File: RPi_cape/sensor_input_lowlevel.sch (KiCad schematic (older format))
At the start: 38 parts, among them U14 DNP, U15 LMC7101B, U16 LMC7101B, U17 LM2903

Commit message: Finished schematic, most of PCB placement
Added error budget for analog inputs
Finished most of PCB placement and started routing
Added R185, R186 to allow powering CPLD from alarm power for better power-down alarm sound flexibility
Changed power-down alarm monitoring from +5VD to +3.3V, and put +5VA and +24VA monitoring as DNP by default, to match the CPLD's ability to run off backup battery and monitor +5VA/+24VA
Moved from 3x AA (4.5V) to 4x AA (6V) alarm battery for better audio voltage, and added PNP diode-ORing circuit (Q12 etc.) to accomodate higher voltage, changed low-battery threshold to 5V
Added pull-down resistors to sensor op-amp outputs to help extend low-end output range
Changed 1nF, 10nF, 100nF caps to 0603-size for better fit of CPLD decoupling caps
Added additional bulk cap C19 to audio amp's supply just in case of alarm-induced supply fluctuations
Decreased CPLD's I2C pull-up values to deal with anticipated PCB capacitance etc.
Removed additional dual-op-amp footprint option on analog inputs, due to high availability of single op-amps
Adjusted O2 sensor input clamping to reduce errors from diode leakage current (changed from zener to low-leakage clamps to rails)
Changed O2 sensor op-amp to different lower-offset part to reduce total error from +/- 4.2% FS to +/- 1.7% FS
Fixed missing power section for U17
Added rotary encoder input
Consolidated +5VA fuse options
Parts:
- removed C40, C43: 1uF 16V X7R, Capacitor_SMD:C_0805_2012Metric, symbol Device:C
- removed U14: DNP, Package_SO:SOIC-8_3.9x4.9mm_P1.27mm, symbol Device:Opamp_Dual_Generic
- removed U15, U16: LMC7101B, Package_TO_SOT_SMD:SOT-23-5, symbol Amplifier_Operational:LMV321
- added C31: 1uF 16V X7R, Capacitor_SMD:C_0805_2012Metric, symbol Device:C
- added R183, R184: 10K, Resistor_SMD:R_1206_3216Metric, symbol Device:R
- added unit 3 of U17
- added U4: AD8552A, Package_SO:SOIC-8_3.9x4.9mm_P1.27mm, symbol Device:Opamp_Dual_Generic
- C41, C44, C45: footprint Capacitor_SMD:C_0805_2012Metric -> Capacitor_SMD:C_0603_1608Metric; Manufacturer Samsung -> Murata; Part Number CL21C103JBFNNNG -> GRM1885C1H103JA01D
- C46, C47: footprint Capacitor_SMD:C_0805_2012Metric -> Capacitor_SMD:C_0603_1608Metric; Part Number 08055C104KAT2A -> 06035C104JAT2A
- D19: value DNP -> BAS21AH; footprint Diode_SMD:D_SOD-123 -> Diode_SMD:D_SOD-323; Manufacturer (none) -> ON Semiconductor; Part Number (none) -> BAS21AHT1G
- D20: value 5.1V -> BAS21AH; footprint Diode_SMD:D_SOD-123 -> Diode_SMD:D_SOD-323; symbol Device:D_Zener_ALT -> Device:D_ALT; Manufacturer (none) -> ON Semiconductor; Part Number (none) -> BAS21AHT1G
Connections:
- net +5VA: now also C31.2, U17.8 (V+), U4.8 (V+)
- net GND: now also C31.1, R183.1, R184.1, U17.4 (V-), U4.4 (V-)
- net Out: now also R183.2, U4.1
- net at R87.1: now also U4.5 (+)
- net at C45.1, R91.1, R92.2: now also R184.2, U4.7
- net at C45.2, R89.2, R91.2: now also U4.6 (-)
- net at R86.1: now also U4.3 (+)
- net at C44.2, R88.2, R90.2: now also U4.2 (-)
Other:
- note added: "Gain of +101 (7 mV in = 0.707V out, 13 mV in = 1.31V out)\nLPF fc = 1.6 kHz"
- note removed: "Gain of +101 (21 mV in = 2.12V out)\nLPF fc = 1.6 kHz"
- moved on the sheet: C42, R87, R88, R89

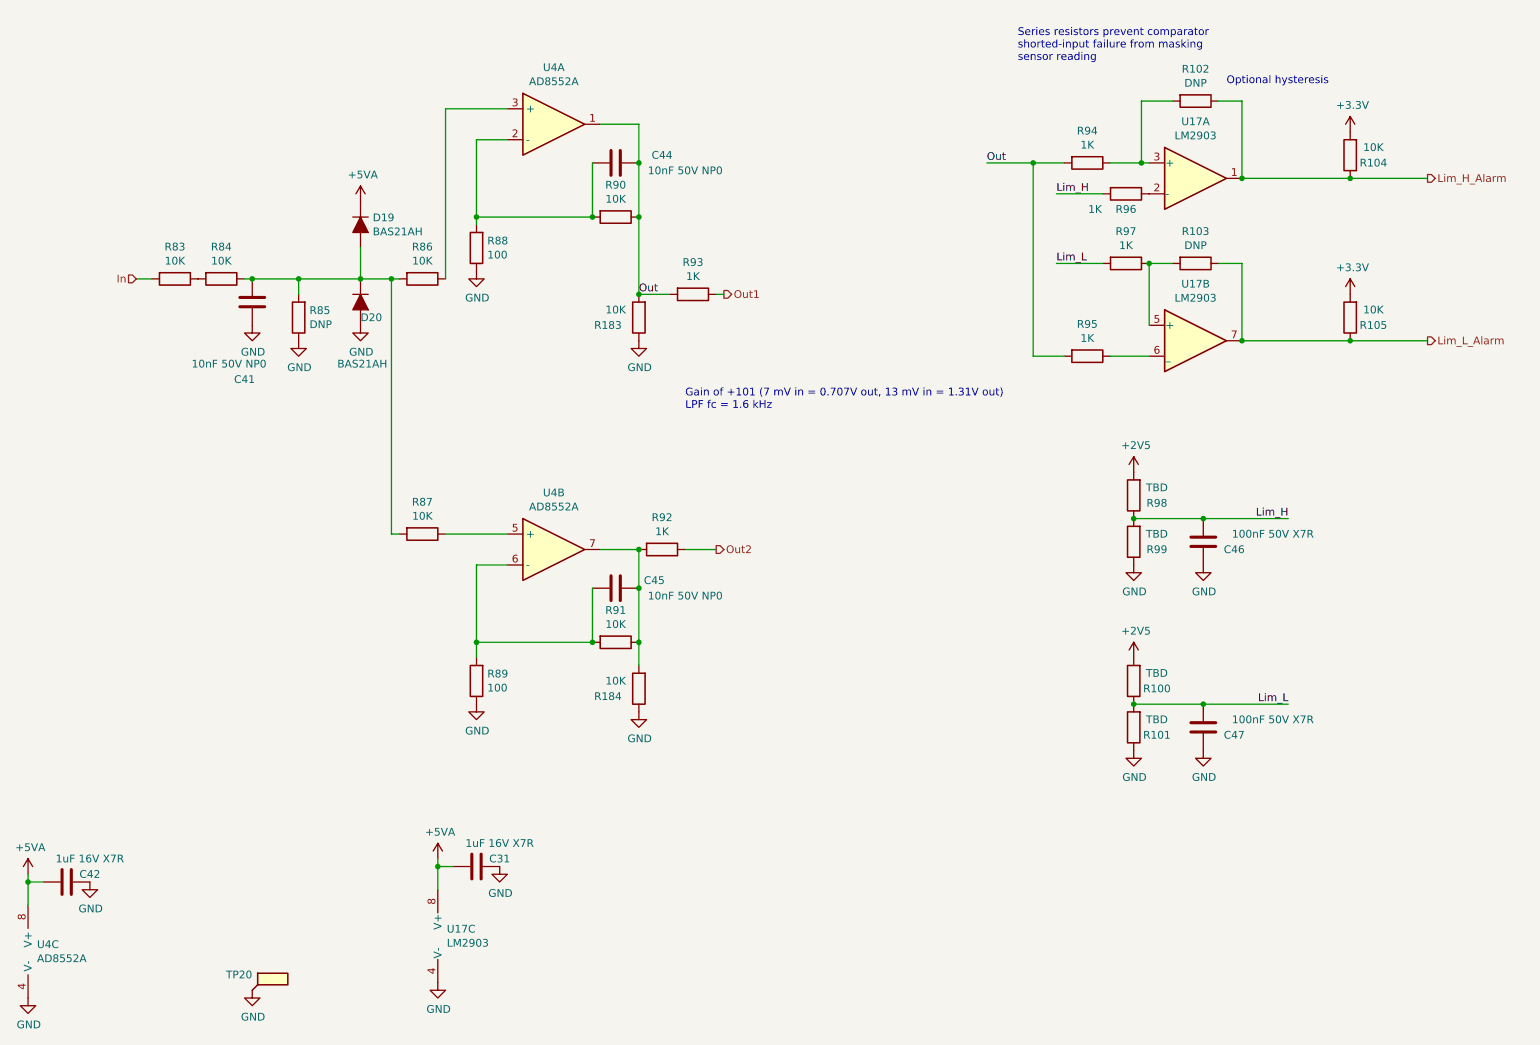
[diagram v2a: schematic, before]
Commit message: Better valve monitoring, finalized layout and manufacturing files
Created assembly and fabrication drawings, assigned all BOM parts, generally made design ready for ordering
Added strain-relief slots and barb mounting dimensions for digital pressure sensors
Changed valve drivers from discrete power MOSFETs to "smart" industrial/automotive driver ICs for the current monitoring, including valve-movement monitor for #4
Connected RPi_Valve* signals to larger CPLD footprint, changed Raspberry Pi pin assignment as a result to ease PCB routing
Updated footprints, page layout to create readable assembly drawing
Added current-measurement testpoints for CPLD power from BATT+
Changed power diodes in power-down-alarm circuit to small-signal parts for more compact layout
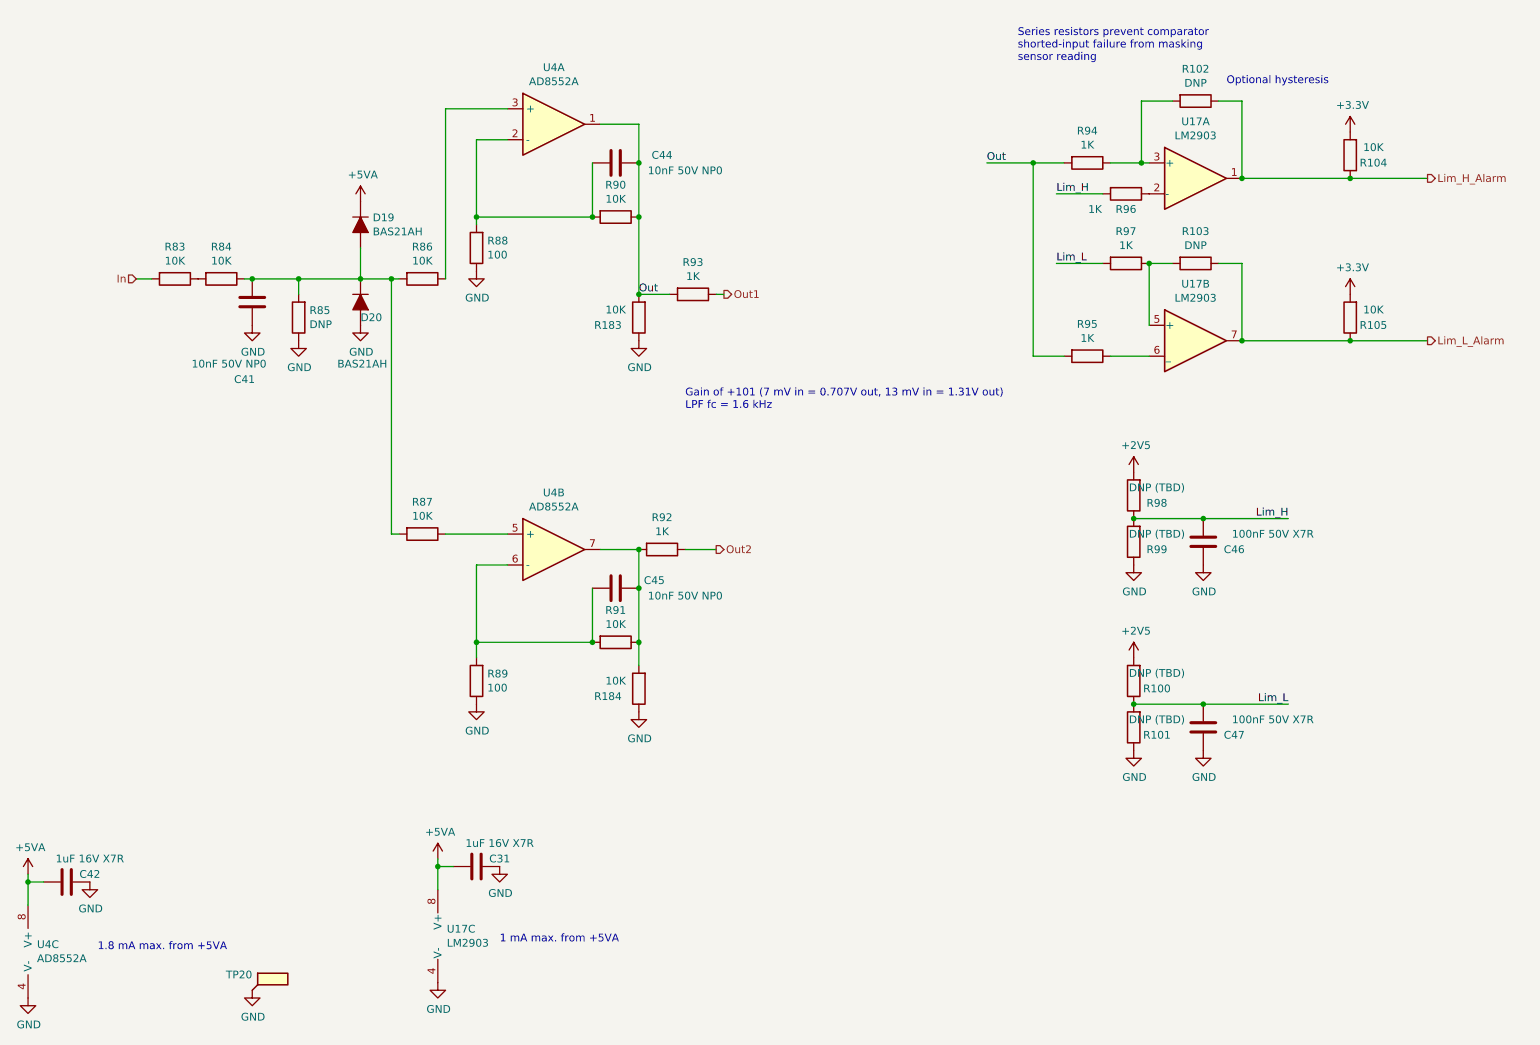
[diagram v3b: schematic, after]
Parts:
- D19, D20: footprint Diode_SMD:D_SOD-323 -> Ventilator:D_SOD-323
- R100, R101, R98, R99: value TBD -> DNP (TBD)
- R104, R105, R183, R184, R83, R84, R86, R87, R90, R91: Manufacturer (none) -> KOA Speer; Part Number (none) -> RK73H2BTTD1002F
- R88, R89: Manufacturer (none) -> KOA Speer; Part Number (none) -> RK73H2BTTD1000F
- R92, R93, R94, R95, R96, R97: Manufacturer (none) -> KOA Speer; Part Number (none) -> RK73H2BTTD1001F
- U17: footprint Package_SO:VSSOP-8_3.0x3.0mm_P0.65mm -> Ventilator:VSSOP-8_3.0x3.0mm_P0.65mm
- U4: footprint Package_SO:SOIC-8_3.9x4.9mm_P1.27mm -> Ventilator:SOIC-8_3.9x4.9mm_P1.27mm
- U4: footprint Package_SO:SOIC-8_3.9x4.9mm_P1.27mm -> Ventilator:SOIC-8_3.9x4.9mm_P1.27mm; Manufacturer (none) -> Analog Devices; Part Number (none) -> AD8552ARZ-REEL
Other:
- note added: "1 mA max. from +5VA"
- note added: "1.8 mA max. from +5VA"
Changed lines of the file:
@@
 $Descr A4 11693 8268
 encoding utf-8
-Sheet 5 14
+Sheet 5 15
 Title "Sensor Input (low-level oxygen sensor)"
 Date ""
@@
 F 2 "Resistor_SMD:R_1206_3216Metric" V 3530 4250 50  0001 C CNN
 F 3 "~" H 3600 4250 50  0001 C CNN
+F 4 "KOA Speer" H 3600 4250 50  0001 C CNN "Manufacturer"
+F 5 "RK73H2BTTD1002F" H 3600 4250 50  0001 C CNN "Part Number"
 	1    3600 4250
 	0    1    1    0
@@
 F 2 "Resistor_SMD:R_1206_3216Metric" V 3880 5200 50  0001 C CNN
 F 3 "~" H 3950 5200 50  0001 C CNN
+F 4 "KOA Speer" H 3950 5200 50  0001 C CNN "Manufacturer"
+F 5 "RK73H2BTTD1000F" H 3950 5200 50  0001 C CNN "Part Number"
 	1    3950 5200
 	-1   0    0    1
@@
 F 2 "Resistor_SMD:R_1206_3216Metric" V 4780 4950 50  0001 C CNN
 F 3 "~" H 4850 4950 50  0001 C CNN
+F 4 "KOA Speer" H 4850 4950 50  0001 C CNN "Manufacturer"
+F 5 "RK73H2BTTD1002F" H 4850 4950 50  0001 C CNN "Part Number"
 	1    4850 4950
 	0    1    1    0
@@
 F 0 "D20" V 3300 2750 50  0000 L CNN
 F 1 "BAS21AH" V 3600 2600 50  0000 L CNN
-F 2 "Diode_SMD:D_SOD-323" H 3200 2750 50  0001 C CNN
+F 2 "Ventilator:D_SOD-323" H 3200 2750 50  0001 C CNN
 F 3 "~" H 3200 2750 50  0001 C CNN
 F 4 "ON Semiconductor" H 3200 2750 50  0001 C CNN "Manufacturer"
@@
 F 2 "Resistor_SMD:R_1206_3216Metric" V 3530 2600 50  0001 C CNN
 F 3 "~" H 3600 2600 50  0001 C CNN
+F 4 "KOA Speer" H 3600 2600 50  0001 C CNN "Manufacturer"
+F 5 "RK73H2BTTD1002F" H 3600 2600 50  0001 C CNN "Part Number"
 	1    3600 2600
 	0    1    1    0
@@
 F 2 "Resistor_SMD:R_1206_3216Metric" V 1930 2600 50  0001 C CNN
 F 3 "~" H 2000 2600 50  0001 C CNN
+F 4 "KOA Speer" H 2000 2600 50  0001 C CNN "Manufacturer"
+F 5 "RK73H2BTTD1002F" H 2000 2600 50  0001 C CNN "Part Number"
 	1    2000 2600
 	0    1    1    0
@@
 F 2 "Resistor_SMD:R_1206_3216Metric" V 2230 2600 50  0001 C CNN
 F 3 "~" H 2300 2600 50  0001 C CNN
+F 4 "KOA Speer" H 2300 2600 50  0001 C CNN "Manufacturer"
+F 5 "RK73H2BTTD1002F" H 2300 2600 50  0001 C CNN "Part Number"
 	1    2300 2600
 	0    1    1    0
@@
 F 2 "Resistor_SMD:R_1206_3216Metric" V 3880 2400 50  0001 C CNN
 F 3 "~" H 3950 2400 50  0001 C CNN
+F 4 "KOA Speer" H 3950 2400 50  0001 C CNN "Manufacturer"
+F 5 "RK73H2BTTD1000F" H 3950 2400 50  0001 C CNN "Part Number"
 	1    3950 2400
 	-1   0    0    1
@@
 F 2 "Resistor_SMD:R_1206_3216Metric" V 4780 2200 50  0001 C CNN
 F 3 "~" H 4850 2200 50  0001 C CNN
+F 4 "KOA Speer" H 4850 2200 50  0001 C CNN "Manufacturer"
+F 5 "RK73H2BTTD1002F" H 4850 2200 50  0001 C CNN "Part Number"
 	1    4850 2200
 	0    1    1    0
@@
 F 2 "Resistor_SMD:R_1206_3216Metric" V 5280 2700 50  0001 C CNN
 F 3 "~" H 5350 2700 50  0001 C CNN
+F 4 "KOA Speer" H 5350 2700 50  0001 C CNN "Manufacturer"
+F 5 "RK73H2BTTD1001F" H 5350 2700 50  0001 C CNN "Part Number"
 	1    5350 2700
 	0    1    1    0
@@
 F 2 "Resistor_SMD:R_1206_3216Metric" V 5080 4350 50  0001 C CNN
 F 3 "~" H 5150 4350 50  0001 C CNN
+F 4 "KOA Speer" H 5150 4350 50  0001 C CNN "Manufacturer"
+F 5 "RK73H2BTTD1001F" H 5150 4350 50  0001 C CNN "Part Number"
 	1    5150 4350
 	0    1    1    0
@@
 F 0 "D19" V 3154 2329 50  0000 L CNN
 F 1 "BAS21AH" V 3245 2329 50  0000 L CNN
-F 2 "Diode_SMD:D_SOD-323" H 3200 2250 50  0001 C CNN
+F 2 "Ventilator:D_SOD-323" H 3200 2250 50  0001 C CNN
 F 3 "~" H 3200 2250 50  0001 C CNN
 F 4 "ON Semiconductor" H 3200 2250 50  0001 C CNN "Manufacturer"
@@
 F 0 "U17" H 8600 2317 50  0000 C CNN
 F 1 "LM2903" H 8600 2226 50  0000 C CNN
-F 2 "Package_SO:VSSOP-8_3.0x3.0mm_P0.65mm" H 8600 1950 50  0001 C CNN
+F 2 "Ventilator:VSSOP-8_3.0x3.0mm_P0.65mm" H 8600 1950 50  0001 C CNN
 F 3 "http://www.ti.com/lit/ds/symlink/lm393-n.pdf" H 8600 1950 50  0001 C CNN
 F 4 "Texas Instruments" H 8600 1950 50  0001 C CNN "Manufacturer"
@@
 F 0 "U17" H 8600 3367 50  0000 C CNN
 F 1 "LM2903" H 8600 3276 50  0000 C CNN
-F 2 "Package_SO:VSSOP-8_3.0x3.0mm_P0.65mm" H 8600 3000 50  0001 C CNN
+F 2 "Ventilator:VSSOP-8_3.0x3.0mm_P0.65mm" H 8600 3000 50  0001 C CNN
 F 3 "http://www.ti.com/lit/ds/symlink/lm393-n.pdf" H 8600 3000 50  0001 C CNN
 F 4 "Texas Instruments" H 8600 3000 50  0001 C CNN "Manufacturer"
@@
 F 2 "Resistor_SMD:R_1206_3216Metric" V 7830 1850 50  0001 C CNN
 F 3 "~" H 7900 1850 50  0001 C CNN
+F 4 "KOA Speer" H 7900 1850 50  0001 C CNN "Manufacturer"
+F 5 "RK73H2BTTD1001F" H 7900 1850 50  0001 C CNN "Part Number"
 	1    7900 1850
 	0    1    1    0
@@
 F 2 "Resistor_SMD:R_1206_3216Metric" V 7830 3100 50  0001 C CNN
 F 3 "~" H 7900 3100 50  0001 C CNN
+F 4 "KOA Speer" H 7900 3100 50  0001 C CNN "Manufacturer"
+F 5 "RK73H2BTTD1001F" H 7900 3100 50  0001 C CNN "Part Number"
 	1    7900 3100
 	0    1    1    0
@@
 F 2 "Resistor_SMD:R_1206_3216Metric" V 9530 1800 50  0001 C CNN
 F 3 "~" H 9600 1800 50  0001 C CNN
+F 4 "KOA Speer" H 9600 1800 50  0001 C CNN "Manufacturer"
+F 5 "RK73H2BTTD1002F" H 9600 1800 50  0001 C CNN "Part Number"
 	1    9600 1800
 	-1   0    0    1
@@
 AR Path="/5E8AA959/5EDD8202" Ref="R98"  Part="1"
 F 0 "R98" H 8050 4050 50  0000 C CNN
-F 1 "TBD" H 8050 3950 50  0000 C CNN
+F 1 "DNP (TBD)" H 8050 3950 50  0000 C CNN
 F 2 "Resistor_SMD:R_1206_3216Metric" V 8130 4000 50  0001 C CNN
 F 3 "~" H 8200 4000 50  0001 C CNN
@@
 AR Path="/5E8AA959/5EDD8208" Ref="R99"  Part="1"
 F 0 "R99" H 8050 4350 50  0000 C CNN
-F 1 "TBD" H 8050 4250 50  0000 C CNN
+F 1 "DNP (TBD)" H 8050 4250 50  0000 C CNN
 F 2 "Resistor_SMD:R_1206_3216Metric" V 8130 4300 50  0001 C CNN
 F 3 "~" H 8200 4300 50  0001 C CNN
@@
 AR Path="/5E8AA959/5EDD822B" Ref="R100"  Part="1"
 F 0 "R100" H 8050 5250 50  0000 C CNN
-F 1 "TBD" H 8050 5150 50  0000 C CNN
+F 1 "DNP (TBD)" H 8050 5150 50  0000 C CNN
 F 2 "Resistor_SMD:R_1206_3216Metric" V 8130 5200 50  0001 C CNN
 F 3 "~" H 8200 5200 50  0001 C CNN
@@
 AR Path="/5E8AA959/5EDD8231" Ref="R101"  Part="1"
 F 0 "R101" H 8050 5550 50  0000 C CNN
-F 1 "TBD" H 8050 5450 50  0000 C CNN
+F 1 "DNP (TBD)" H 8050 5450 50  0000 C CNN
 F 2 "Resistor_SMD:R_1206_3216Metric" V 8130 5500 50  0001 C CNN
 F 3 "~" H 8200 5500 50  0001 C CNN
@@
 F 2 "Resistor_SMD:R_1206_3216Metric" V 8080 2500 50  0001 C CNN
 F 3 "~" H 8150 2500 50  0001 C CNN
+F 4 "KOA Speer" H 8150 2500 50  0001 C CNN "Manufacturer"
+F 5 "RK73H2BTTD1001F" H 8150 2500 50  0001 C CNN "Part Number"
 	1    8150 2500
 	0    1    1    0
@@
 F 2 "Resistor_SMD:R_1206_3216Metric" V 8080 2050 50  0001 C CNN
 F 3 "~" H 8150 2050 50  0001 C CNN
+F 4 "KOA Speer" H 8150 2050 50  0001 C CNN "Manufacturer"
+F 5 "RK73H2BTTD1001F" H 8150 2050 50  0001 C CNN "Part Number"
 	1    8150 2050
 	0    1    1    0
@@
 F 2 "Resistor_SMD:R_1206_3216Metric" V 9530 2850 50  0001 C CNN
 F 3 "~" H 9600 2850 50  0001 C CNN
+F 4 "KOA Speer" H 9600 2850 50  0001 C CNN "Manufacturer"
+F 5 "RK73H2BTTD1002F" H 9600 2850 50  0001 C CNN "Part Number"
 	1    9600 2850
 	-1   0    0    1
@@
 F 2 "Resistor_SMD:R_1206_3216Metric" V 4930 2850 50  0001 C CNN
 F 3 "~" H 5000 2850 50  0001 C CNN
+F 4 "KOA Speer" H 5000 2850 50  0001 C CNN "Manufacturer"
+F 5 "RK73H2BTTD1002F" H 5000 2850 50  0001 C CNN "Part Number"
 	1    5000 2850
 	-1   0    0    1
@@
 F 2 "Resistor_SMD:R_1206_3216Metric" V 4930 5250 50  0001 C CNN
 F 3 "~" H 5000 5250 50  0001 C CNN
+F 4 "KOA Speer" H 5000 5250 50  0001 C CNN "Manufacturer"
+F 5 "RK73H2BTTD1002F" H 5000 5250 50  0001 C CNN "Part Number"
 	1    5000 5250
 	-1   0    0    1
@@
 F 0 "U4" H 4450 1967 50  0000 C CNN
 F 1 "AD8552A" H 4450 1876 50  0000 C CNN
-F 2 "Package_SO:SOIC-8_3.9x4.9mm_P1.27mm" H 4450 1600 50  0001 C CNN
+F 2 "Ventilator:SOIC-8_3.9x4.9mm_P1.27mm" H 4450 1600 50  0001 C CNN
 F 3 "~" H 4450 1600 50  0001 C CNN
 F 4 "Analog Devices" H 4450 1600 50  0001 C CNN "Manufacturer"
@@
 F 0 "U4" H 4450 4717 50  0000 C CNN
 F 1 "AD8552A" H 4450 4626 50  0000 C CNN
-F 2 "Package_SO:SOIC-8_3.9x4.9mm_P1.27mm" H 4450 4350 50  0001 C CNN
+F 2 "Ventilator:SOIC-8_3.9x4.9mm_P1.27mm" H 4450 4350 50  0001 C CNN
 F 3 "~" H 4450 4350 50  0001 C CNN
+F 4 "Analog Devices" H 4450 4350 50  0001 C CNN "Manufacturer"
+F 5 "AD8552ARZ-REEL" H 4450 4350 50  0001 C CNN "Part Number"
 	2    4450 4350
 	1    0    0    -1
@@
 F 0 "U4" H 1108 6996 50  0000 L CNN
 F 1 "AD8552A" H 1108 6905 50  0000 L CNN
-F 2 "Package_SO:SOIC-8_3.9x4.9mm_P1.27mm" H 1150 6950 50  0001 C CNN
+F 2 "Ventilator:SOIC-8_3.9x4.9mm_P1.27mm" H 1150 6950 50  0001 C CNN
 F 3 "~" H 1150 6950 50  0001 C CNN
+F 4 "Analog Devices" H 1150 6950 50  0001 C CNN "Manufacturer"
+F 5 "AD8552ARZ-REEL" H 1150 6950 50  0001 C CNN "Part Number"
 	3    1150 6950
 	1    0    0    -1
@@
 F 0 "U17" H 3758 6896 50  0000 L CNN
 F 1 "LM2903" H 3758 6805 50  0000 L CNN
-F 2 "Package_SO:VSSOP-8_3.0x3.0mm_P0.65mm" H 3800 6850 50  0001 C CNN
+F 2 "Ventilator:VSSOP-8_3.0x3.0mm_P0.65mm" H 3800 6850 50  0001 C CNN
 F 3 "http://www.ti.com/lit/ds/symlink/lm393-n.pdf" H 3800 6850 50  0001 C CNN
 F 4 "Texas Instruments" H 3800 6850 50  0001 C CNN "Manufacturer"
@@
 	1    0    0    -1
 $EndComp
+Text Notes 1500 6950 0    50   ~ 0
+1.8 mA max. from +5VA
+Text Notes 4100 6900 0    50   ~ 0
+1 mA max. from +5VA
 $EndSCHEMATC
